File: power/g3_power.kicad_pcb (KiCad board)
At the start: 4 copper layers, 50 x 40 mm, 55 parts, among them J101 533980271_Molex, J102 533980271_Molex, J103 53398-0871, SW101 SW_Push, U101 RT9471GQW, U102 TPS61202DRC, U103 LM358, U104 MCP3422

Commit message: Adding logo
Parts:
- added G***: LOGO, Perch:perch_logo, F.Cu at (242.2, 100.5)

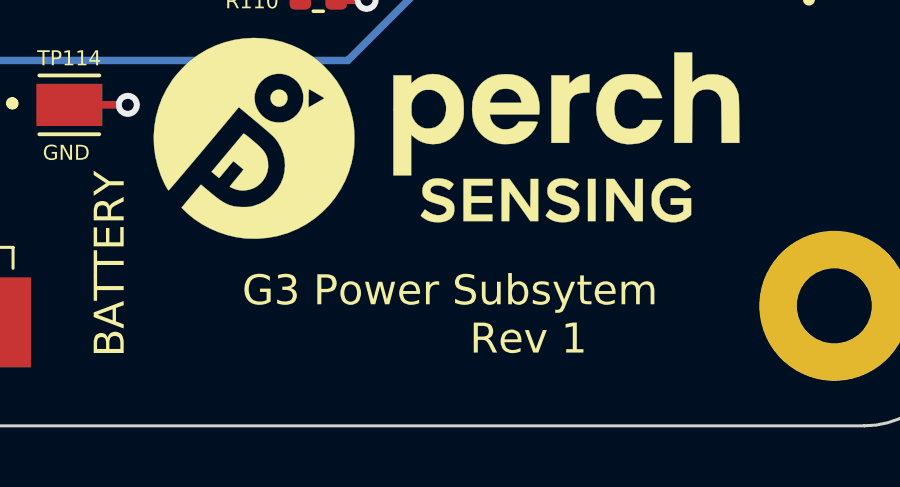
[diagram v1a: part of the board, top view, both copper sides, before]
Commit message: Renaming boards
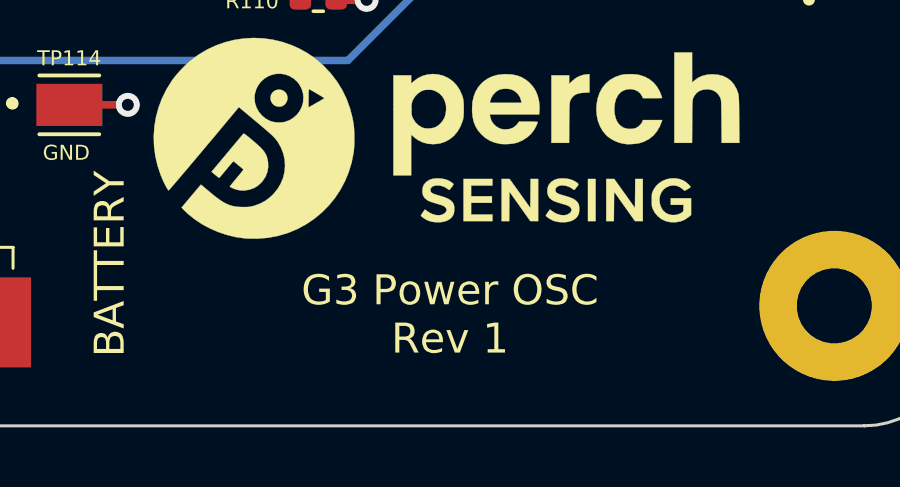
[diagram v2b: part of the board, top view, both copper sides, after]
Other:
- board text added: "G3 Power OSC Rev 1"
- board text removed: "G3 Power Subsytem Rev 1"
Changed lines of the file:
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@@
     (effects (font (size 0.5 0.5) (thickness 0.1)))
   )
-  (gr_text "G3 Power Subsytem\n            Rev 1" (at 242.19 106.29) (layer F.SilkS)
+  (gr_text "G3 Power OSC\nRev 1" (at 242.19 106.29) (layer F.SilkS)
     (effects (font (size 1 1) (thickness 0.25)))
   )

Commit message: Making review 2 changes
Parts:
- TP101, TP102, TP104, TP108, TP109, TP111, TP112: moved to F.Cu
- moved TP108 14.2 mm to (241.2, 81.5), turned to 90 degrees
- moved TP109 12.2 mm to (238.4, 81.2), turned to 90 degrees
- moved TP101 8.58 mm to (233.5, 92.1), turned to 0 degrees
- moved TP102 2.20 mm to (214.6, 84.3), turned to 270 degrees
- moved TP103 2.16 mm to (217.1, 77.0), turned to 270 degrees
- moved TP111 1.76 mm to (216.7, 91.6), turned to 180 degrees
- moved TP104 1.70 mm to (218.0, 80.9), turned to 270 degrees
- moved TP110 1.30 mm to (236.4, 78.7), turned to 90 degrees
- moved JP2 1.09 mm to (211.3, 91.4)
- moved JP1 1.08 mm to (211.3, 84.3)
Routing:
- net BOOST_VAUX: track 12.9 -> 19.4 mm
- net V_SOL: track 37.4 -> 40.5 mm
- net +5V: track 12.9 -> 11.3 mm
- net V_REGN: track 13.4 -> 14.4 mm
- net /VSolSense: track 12.6 -> 13.4 mm
- net GND: track 58.8 -> 59.7 mm
- net /SCL: track 49.9 -> 50.5 mm
- net /SDA: track 44.6 -> 44.0 mm
- net /BOOST_PS: track 30.6 -> 30.0 mm
- net Net-(D101-Pad1): track 6.76 -> 7.28 mm
